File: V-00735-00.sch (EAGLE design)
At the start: 32 parts, among them IC2 MAX481CSA, IC3 FT232RL, IC8 ATMEGA644A, Q1 14.7456MHz, X1 MINI-USB-SCHIELD-32005-201

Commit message: v1.1.0.2
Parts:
- IC8: value ATMEGA644A -> ATMEGA644P; device atmel:ATMEGA644A -> atmel:ATMEGA644P
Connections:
- net RS485_EN: now also IC8.(PCINT28/XCK1/OC1B)PD4; no longer IC8.(PCINT28/OC1B)PD4
- net RS485_RX: now also IC8.(PCINT26/RXD1/INT0)PD2; no longer IC8.(PCINT26/INT0)PD2
- net RS485_TX: now also IC8.(PCINT27/TXD1/INT1)PD3; no longer IC8.(PCINT27/INT1)PD3
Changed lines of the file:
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@@
 <part name="R15" library="#PaJa_31" deviceset="R" device="_1206" value="580R"/>
 <part name="FRAME2" library="frames" deviceset="A4L-LOC" device=""/>
-<part name="IC8" library="atmel" deviceset="ATMEGA644" device="A"/>
+<part name="IC8" library="atmel" deviceset="ATMEGA644P" device=""/>
 <part name="JUM1" library="#PaJa_konektory" deviceset="S1G3_JUMP" device=""/>
 <part name="JUM2" library="#PaJa_konektory" deviceset="S1G4_JUMP" device=""/>
@@
 </segment>
 <segment>
-<pinref part="IC8" gate="G$1" pin="(PCINT28/OC1B)PD4"/>
+<pinref part="IC8" gate="G$1" pin="(PCINT28/XCK1/OC1B)PD4"/>
 <wire x1="137.16" y1="73.66" x2="152.4" y2="73.66" width="0.1524" layer="91"/>
 <label x="152.4" y="73.66" size="1.016" layer="95" font="vector" ratio="10" xref="yes"/>
@@
 </segment>
 <segment>
-<pinref part="IC8" gate="G$1" pin="(PCINT26/INT0)PD2"/>
+<pinref part="IC8" gate="G$1" pin="(PCINT26/RXD1/INT0)PD2"/>
 <wire x1="137.16" y1="68.58" x2="152.4" y2="68.58" width="0.1524" layer="91"/>
 <label x="152.4" y="68.58" size="1.016" layer="95" font="vector" ratio="10" xref="yes"/>
@@
 </segment>
 <segment>
-<pinref part="IC8" gate="G$1" pin="(PCINT27/INT1)PD3"/>
+<pinref part="IC8" gate="G$1" pin="(PCINT27/TXD1/INT1)PD3"/>
 <wire x1="137.16" y1="71.12" x2="152.4" y2="71.12" width="0.1524" layer="91"/>
 <label x="152.4" y="71.12" size="1.016" layer="95" font="vector" ratio="10" xref="yes"/>

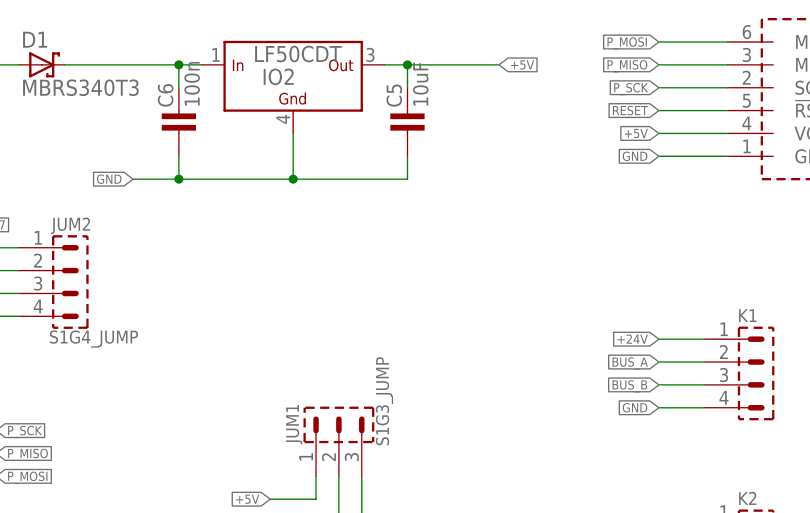
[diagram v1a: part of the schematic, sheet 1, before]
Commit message: v1.1.0.3
Opraveny spoje, nevím proč ale byli divně pospojované. Ale plošnák OK.
ALe nastal problém v stabilizátoru. Blbec jsem si nevšiml vstupního
napájení které pro použitej stabilizátor je pouze 16V proto je nutné ho
nahradit například 78L05-TO92
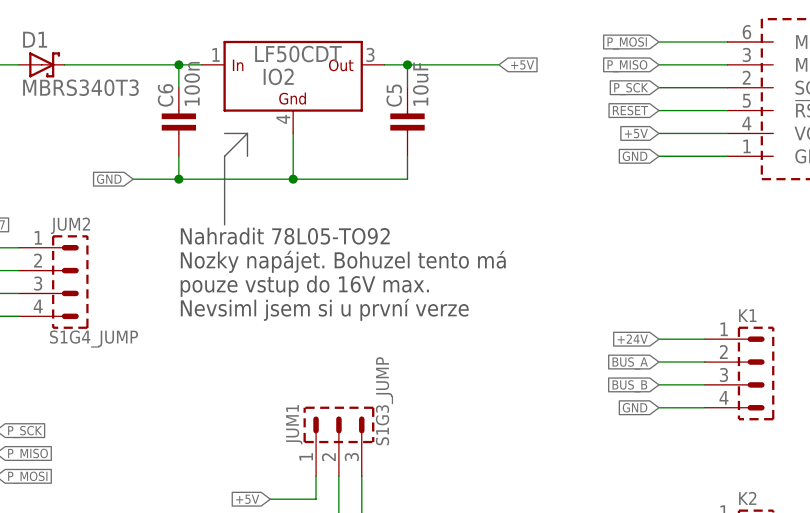
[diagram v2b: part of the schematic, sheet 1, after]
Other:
- note added: "Nahradit 78L05-TO92 Nozky napájet. Bohuzel tento má pouze vstup do 16V max. Nevsiml jsem si u první verze"
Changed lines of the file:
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@@
 RS485 -&gt; 5TTL</text>
 <text x="246.38" y="5.08" size="2.54" layer="94">00</text>
+<text x="165.1" y="139.7" size="1.778" layer="97">Nahradit 78L05-TO92
+Nozky napájet. Bohuzel tento má
+pouze vstup do 16V max.
+Nevsiml jsem si u první verze</text>
+<wire x1="170.18" y1="149.86" x2="170.18" y2="157.48" width="0.1524" layer="97"/>
+<wire x1="170.18" y1="157.48" x2="172.72" y2="160.02" width="0.1524" layer="97"/>
+<wire x1="172.72" y1="160.02" x2="170.18" y2="160.02" width="0.1524" layer="97"/>
+<wire x1="172.72" y1="160.02" x2="172.72" y2="157.48" width="0.1524" layer="97"/>
 </plain>
 <instances>
